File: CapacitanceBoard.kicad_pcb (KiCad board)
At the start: 2 copper layers, 1 part

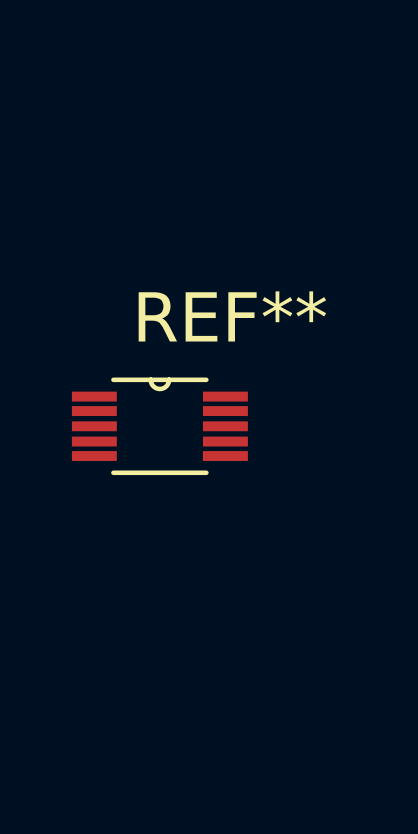
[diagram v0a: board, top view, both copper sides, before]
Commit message: Added Connectors to PCB
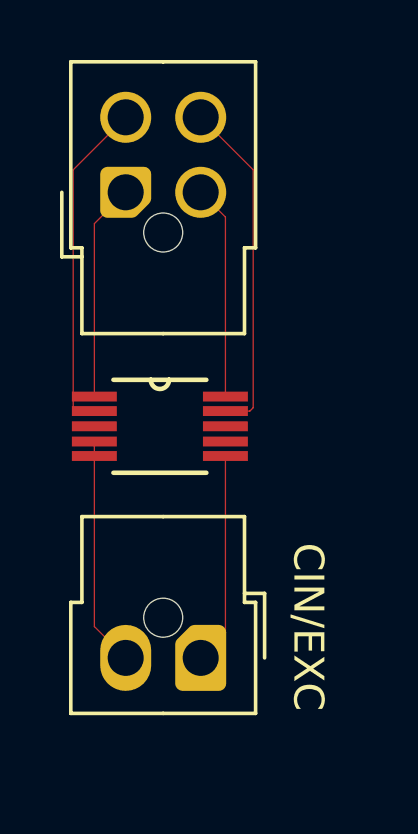
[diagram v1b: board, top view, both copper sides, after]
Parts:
- added REF**: Molex_Nano-Fit_105310-xx04_2x02_P2.50mm_Vertical, Connector_Molex:Molex_Nano-Fit_105310-xx04_2x02_P2.50mm_Vertical, F.Cu at (166.5, 126.8)
- added REF**: Molex_Nano-Fit_105309-xx02_1x02_P2.50mm_Vertical, Connector_Molex:Molex_Nano-Fit_105309-xx02_1x02_P2.50mm_Vertical, F.Cu at (169.0, 142.3)
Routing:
- net (no net): track 0.00 -> 51.6 mm
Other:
- board text added: "CIN/EXC"

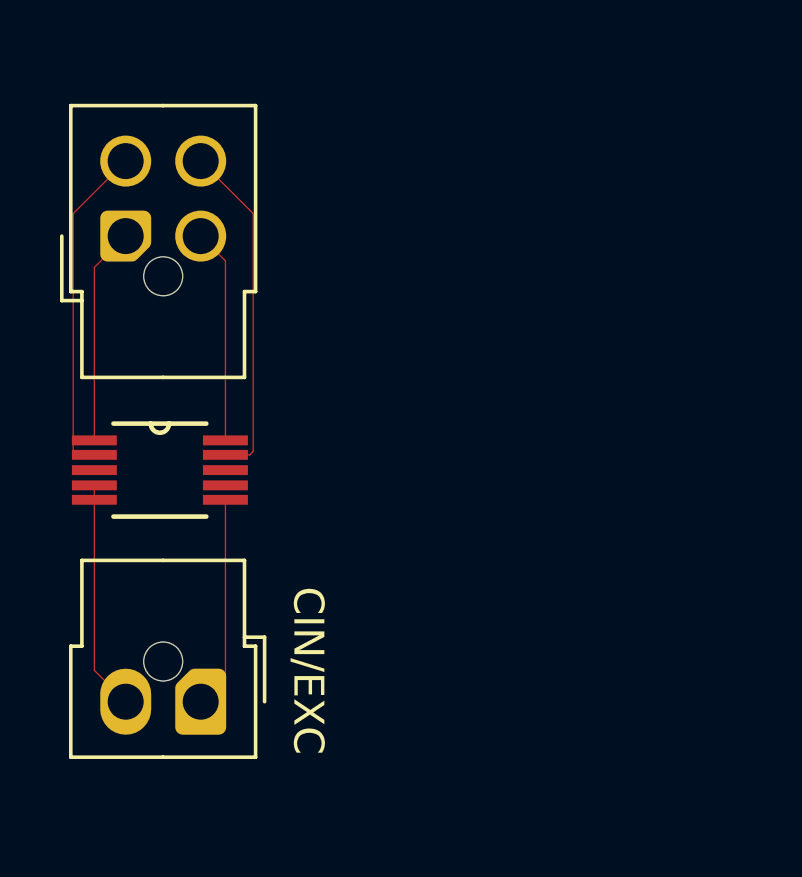
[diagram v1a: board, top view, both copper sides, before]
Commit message: Added Decoupling Capacitor.
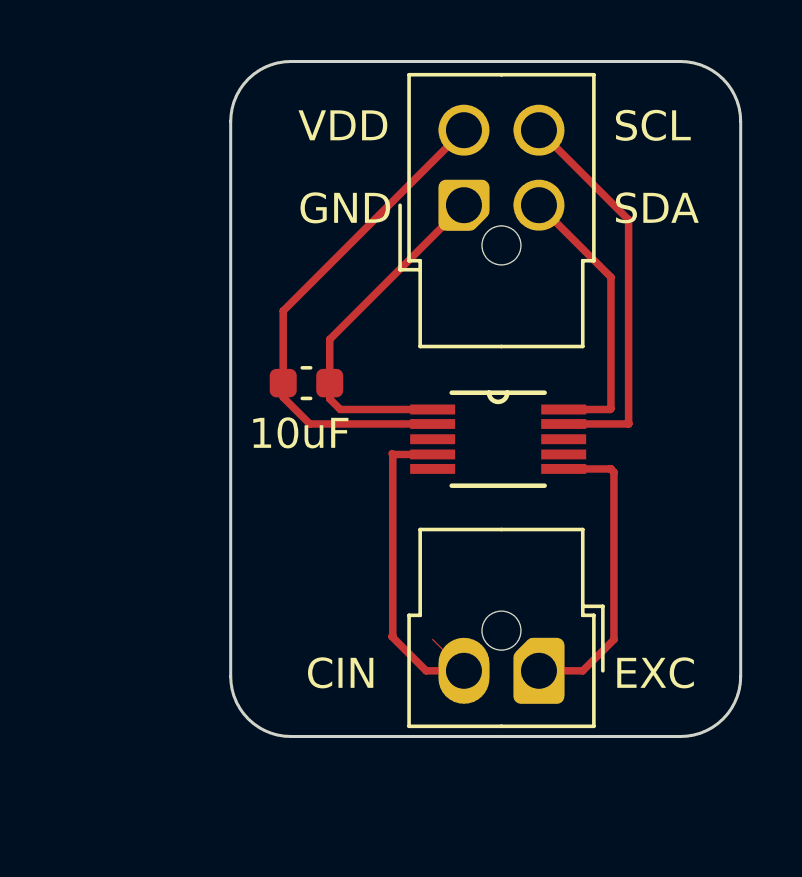
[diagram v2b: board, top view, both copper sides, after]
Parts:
- added REF**: C_0603_1608Metric, Capacitor_SMD:C_0603_1608Metric, F.Cu at (172.5, 131.7)
- moved REF** 11.3 mm to (178.9, 133.6)
- moved REF** 11.3 mm to (177.8, 125.8)
- moved REF** 11.3 mm to (180.3, 141.3)
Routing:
- net (no net): track 51.6 -> 78.0 mm
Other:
- board outline added: 17 x 22.5 mm
- board text added: "10uF"
- board text added: "CIN"
- board text added: "EXC"
- board text added: "GND"
- board text added: "SCL"
- board text added: "SDA"
- board text added: "VDD"
- board text removed: "CIN/EXC"

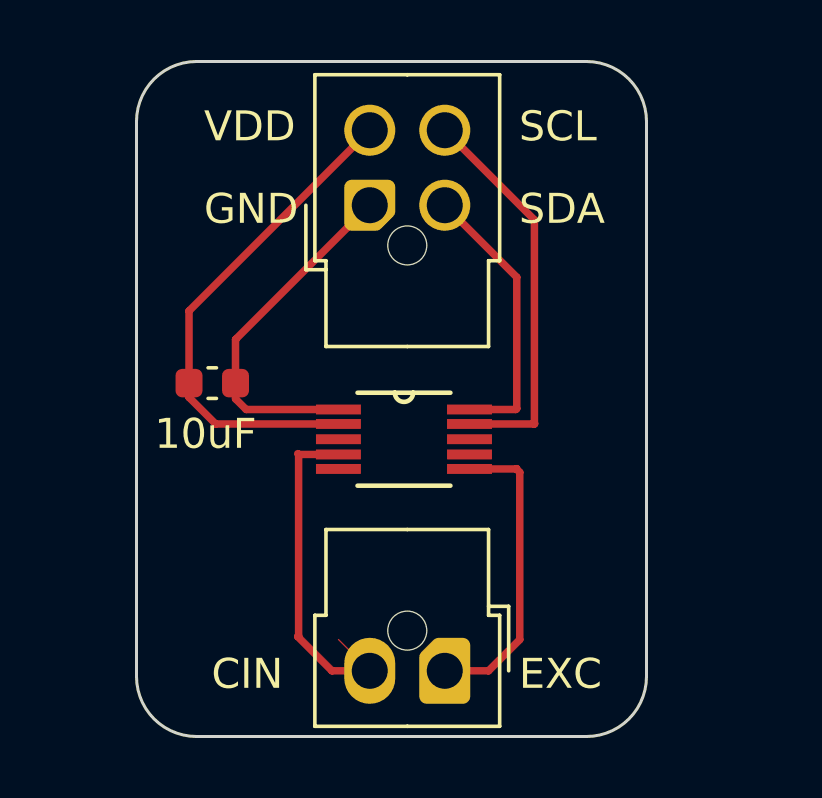
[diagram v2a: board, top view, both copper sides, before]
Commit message: Added Mounting Holes
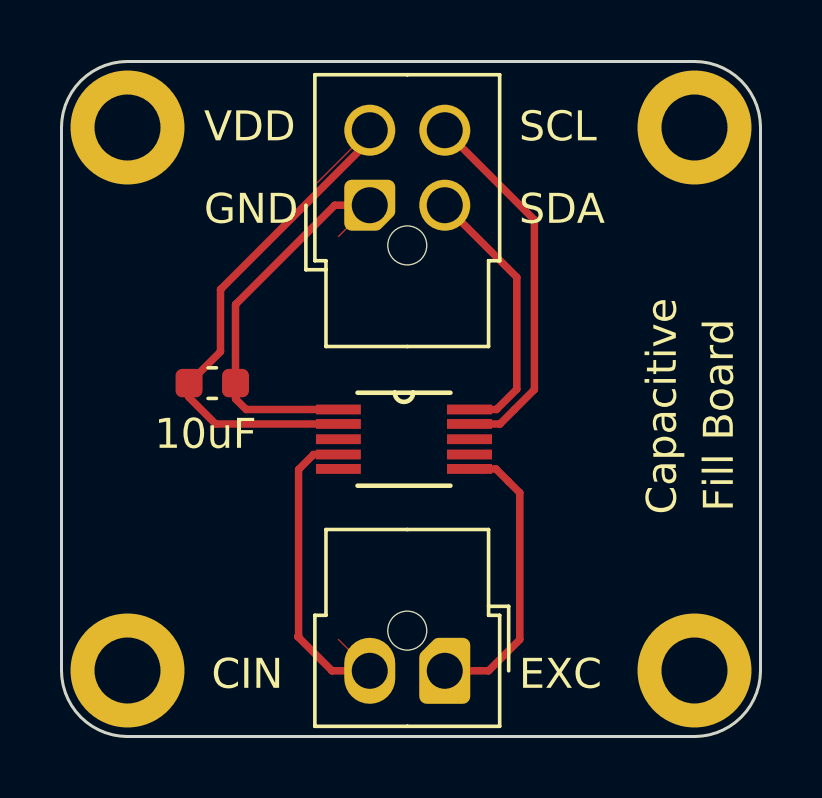
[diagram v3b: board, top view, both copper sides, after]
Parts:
- added REF**: MountingHole_2.2mm_M2_DIN965_Pad, MountingHole:MountingHole_2.2mm_M2_DIN965_Pad, F.Cu at (169.7, 141.3)
- added REF**: MountingHole_2.2mm_M2_DIN965_Pad, MountingHole:MountingHole_2.2mm_M2_DIN965_Pad, F.Cu at (188.6, 123.2)
- added REF**: MountingHole_2.2mm_M2_DIN965_Pad, MountingHole:MountingHole_2.2mm_M2_DIN965_Pad, F.Cu at (188.6, 141.3)
- added REF**: MountingHole_2.2mm_M2_DIN965_Pad, MountingHole:MountingHole_2.2mm_M2_DIN965_Pad, F.Cu at (169.7, 123.2)
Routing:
- net (no net): track 78.0 -> 76.8 mm
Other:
- board size 17 x 22.5 mm -> 23.3 x 22.5 mm
- board text added: "Capacitive"
- board text added: "Fill Board"

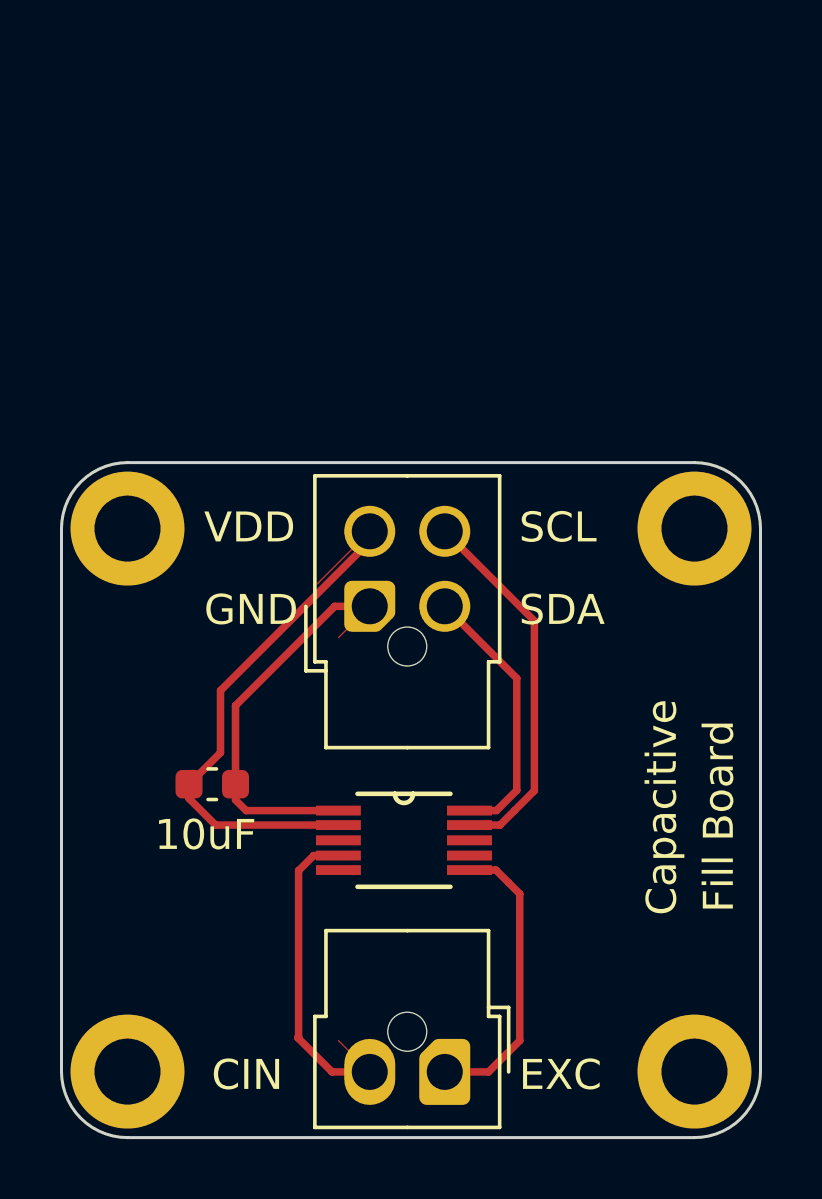
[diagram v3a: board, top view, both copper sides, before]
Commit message: Changed Connector Type to JST-XH
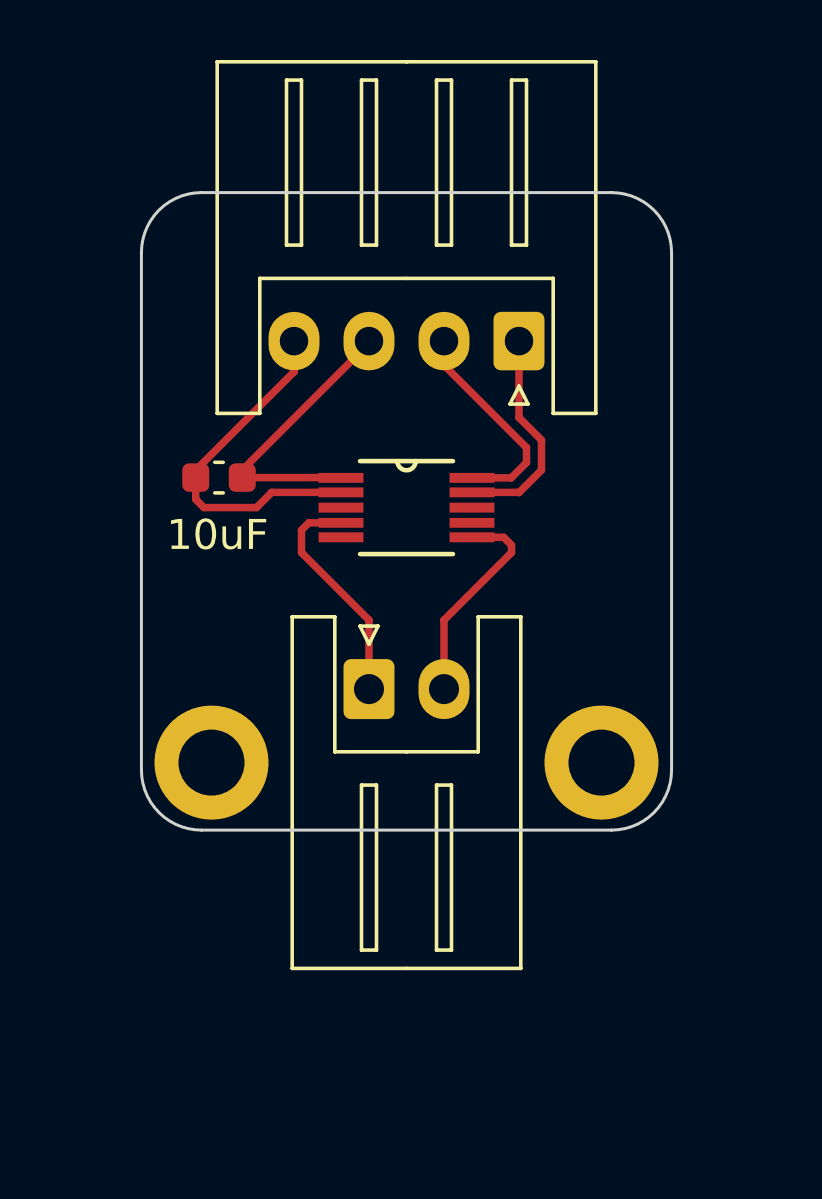
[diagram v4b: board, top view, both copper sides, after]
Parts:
- removed the REF** at (169.7, 141.3)
- removed the REF** at (188.6, 123.2)
- removed the REF** at (177.8, 125.8)
- removed the REF** at (188.6, 141.3)
- removed the REF** at (169.7, 123.2)
- removed the REF** at (180.3, 141.3)
- added REF**: JST_XH_S4B-XH-A_1x04_P2.50mm_Horizontal, Connector_JST:JST_XH_S4B-XH-A_1x04_P2.50mm_Horizontal, F.Cu at (182.8, 117.0)
- added REF**: MountingHole_2.2mm_M2_DIN965_Pad, MountingHole:MountingHole_2.2mm_M2_DIN965_Pad, F.Cu at (185.5, 131.0)
- added REF**: MountingHole_2.2mm_M2_DIN965_Pad, MountingHole:MountingHole_2.2mm_M2_DIN965_Pad, F.Cu at (172.5, 131.0)
- added REF**: JST_XH_S2B-XH-A_1x02_P2.50mm_Horizontal, Connector_JST:JST_XH_S2B-XH-A_1x02_P2.50mm_Horizontal, F.Cu at (177.8, 128.6)
- moved REF** 11.1 mm to (179.0, 122.5)
- moved REF** 10.2 mm to (172.8, 121.5)
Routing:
- net (no net): track 76.8 -> 50.2 mm
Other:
- board size 23.3 x 22.5 mm -> 17.7 x 21.2 mm
- board text removed: "CIN"
- board text removed: "Capacitive"
- board text removed: "EXC"
- board text removed: "Fill Board"
- board text removed: "GND"
- board text removed: "SCL"
- board text removed: "SDA"
- board text removed: "VDD"
